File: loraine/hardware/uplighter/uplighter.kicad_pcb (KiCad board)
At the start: 2 copper layers, 49.5 x 49.5 mm, 10 parts, among them K1 CONN_3, K2 CONN_3, K3 CONN_3, U1 TL4242, U2 TL4242, U3 TL4242

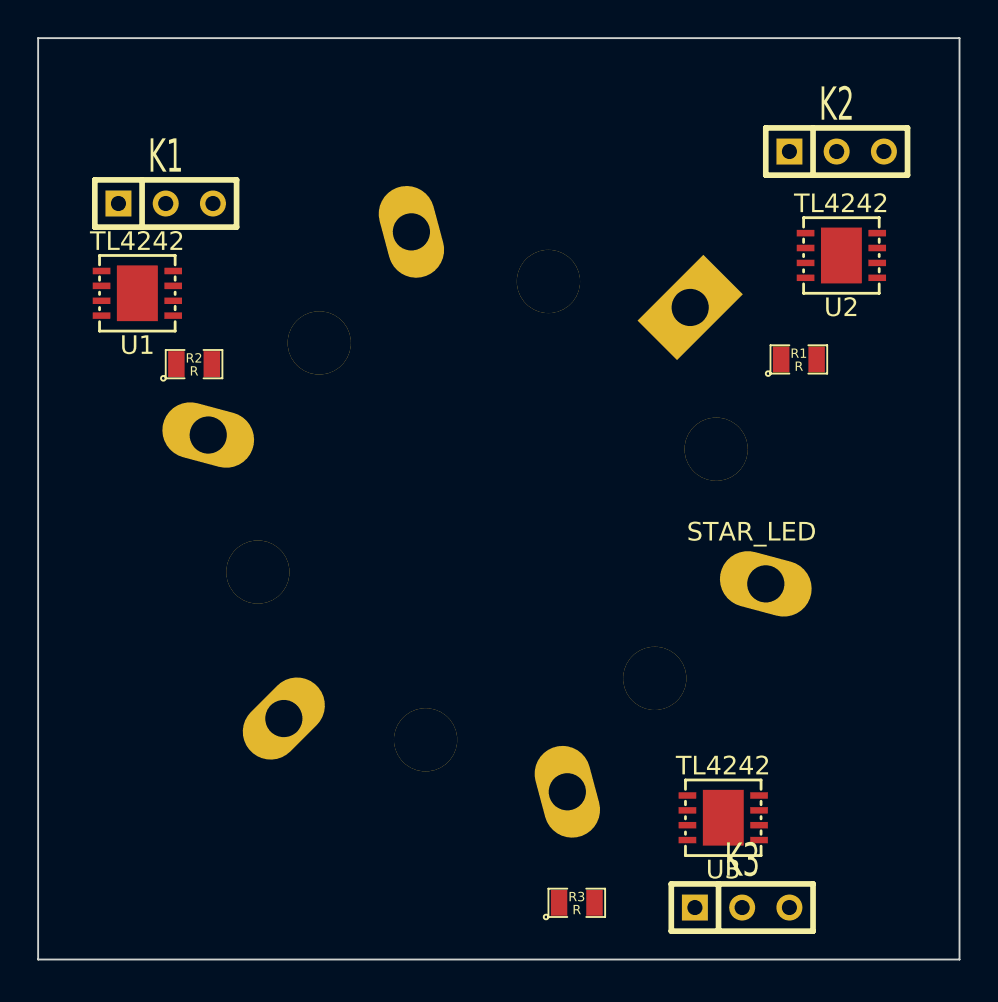
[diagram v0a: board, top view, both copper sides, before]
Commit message: Proposed output driver for node h/w
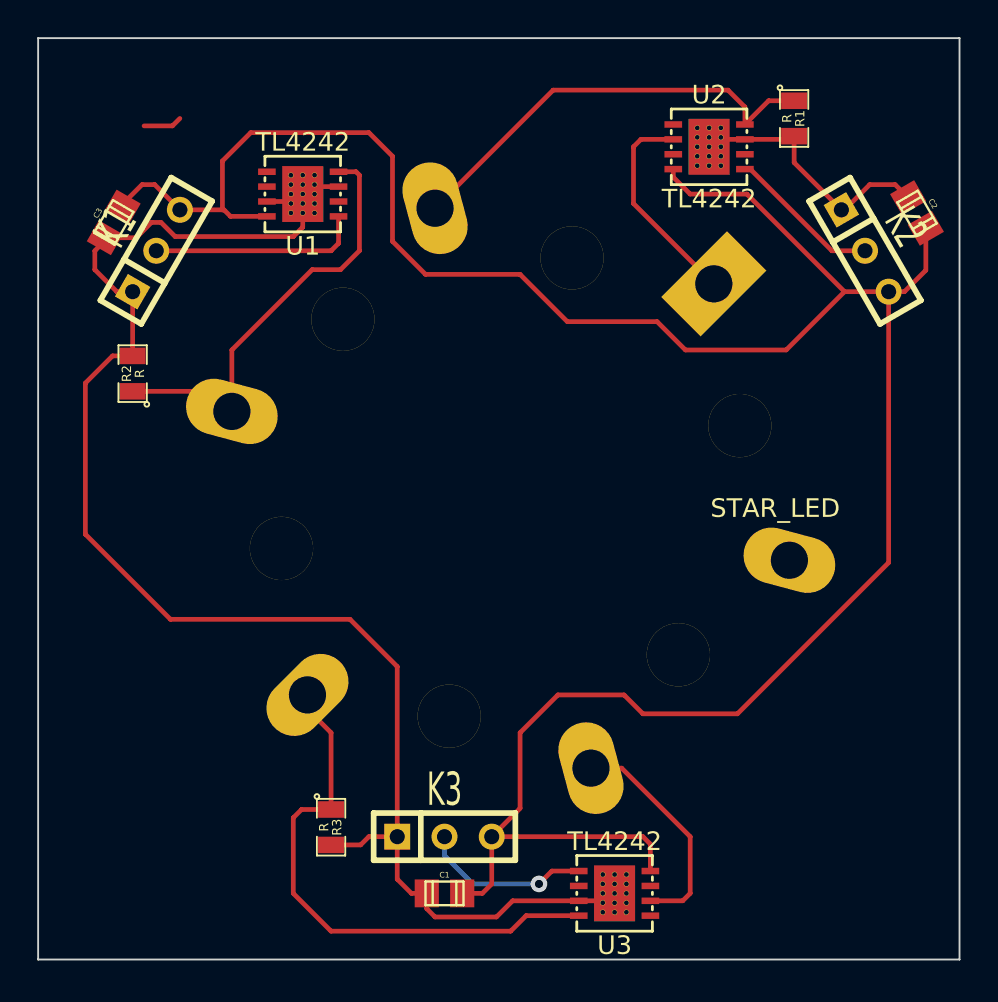
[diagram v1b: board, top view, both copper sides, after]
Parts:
- added C1: C, Capacitors_SMD:c_0805, F.Cu at (220.0, 87.9)
- added C2: C, Capacitors_SMD:c_0805, F.Cu at (245.4, 51.3)
- added C3: C, Capacitors_SMD:c_0805, F.Cu at (202.2, 51.8)
- moved K3 16.4 mm to (220.0, 84.8)
- moved R3 13.8 mm to (213.9, 84.3), turned to 270 degrees
- moved R1 13.0 mm to (238.8, 46.2), turned to 270 degrees
- moved U1 10.4 mm to (212.3, 50.3)
- moved U2 9.20 mm to (234.2, 47.8), turned to 180 degrees
- moved U3 7.12 mm to (229.1, 87.9)
- moved K2 5.55 mm to (242.6, 53.3), turned to 300 degrees
- moved R2 3.34 mm to (203.2, 59.9), turned to 90 degrees
- moved K1 2.59 mm to (204.5, 53.3), turned to 60 degrees
- moved D1 1.80 mm to (223.5, 66.0)
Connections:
- K1 pad 3: Net-(K1-Pad3) -> +5V
- K2 pad 3: Net-(K2-Pad3) -> +5V
- K3 pad 3: Net-(K3-Pad3) -> +5V
- U1 pad 8: Net-(K1-Pad3) -> +5V
- U2 pad 8: Net-(K2-Pad3) -> +5V
- U3 pad 8: Net-(K3-Pad3) -> +5V
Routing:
- net +5V: track 0.00 -> 127.5 mm
- net GND: track 0.00 -> 99.3 mm
- net /REF_RED: track 0.00 -> 29.8 mm
- net /REF_BLUE: track 0.00 -> 29.5 mm
- net /REF_GREEN: track 0.00 -> 23.8 mm
- net /LED_BLUE: track 0.00 -> 12.2 mm
- net /LED_GREEN: track 0.00 -> 11.5 mm
- net Net-(K1-Pad2): track 0.00 -> 10.2 mm
- net Net-(K3-Pad2): track 0.00 -> 9.15 mm, vias 0 -> 1
- net Net-(K2-Pad2): track 0.00 -> 8.27 mm
- net (no net): track 0.00 -> 2.09 mm
- net Net-(U1-Pad5): track 0.00 -> 1.45 mm

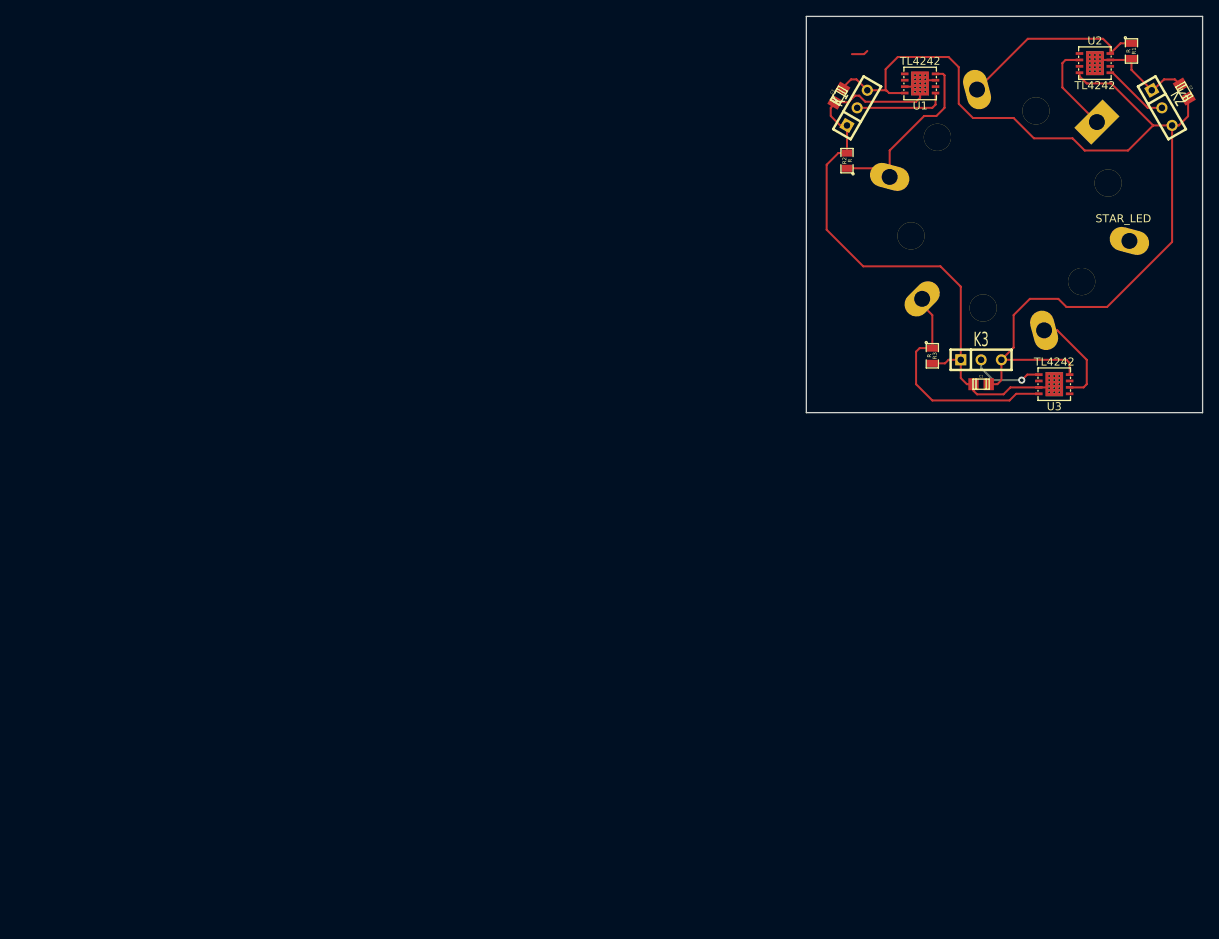
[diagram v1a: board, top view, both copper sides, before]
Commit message: Node PCB redo
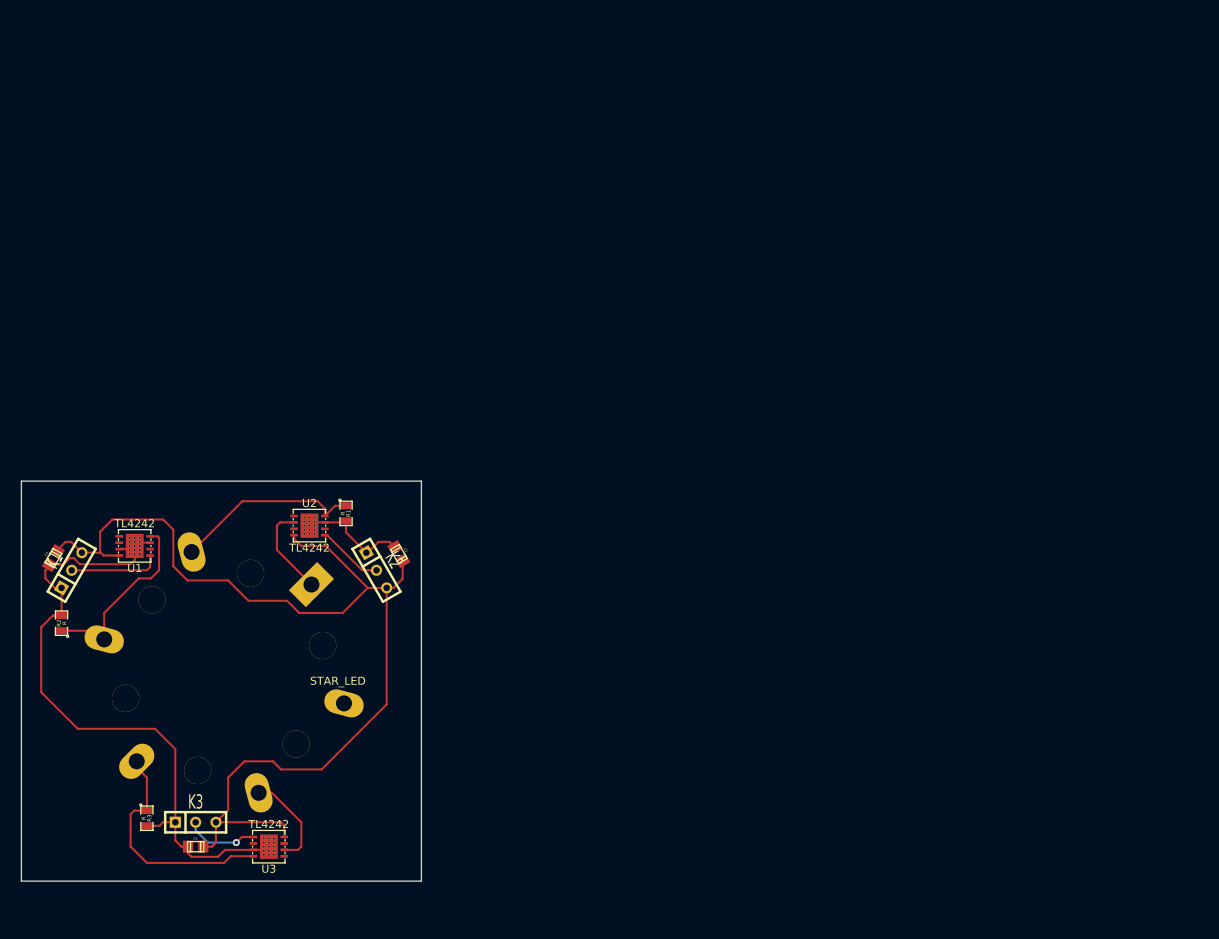
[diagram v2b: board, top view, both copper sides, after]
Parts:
- moved U3 113.9 mm to (130.9, 145.7)
- moved C1 113.9 mm to (121.8, 145.7)
- moved C2 113.9 mm to (147.2, 109.1)
- moved D1 113.9 mm to (125.3, 123.8)
- moved K2 113.9 mm to (144.4, 111.1)
- moved K3 113.9 mm to (121.8, 142.6)
- moved C3 113.9 mm to (104.0, 109.6)
- moved K1 113.9 mm to (106.3, 111.1)
- moved R1 113.9 mm to (140.6, 104.0)
- moved R2 113.9 mm to (105.0, 117.8)
- moved R3 113.9 mm to (115.7, 142.1)
- moved U1 113.9 mm to (114.2, 108.1)
- moved U2 113.9 mm to (136.0, 105.6)
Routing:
- net /REF_RED: track 29.8 -> 77.7 mm
- net +5V: track 127.5 -> 79.6 mm
- net (no net): track 2.09 -> 0.00 mm
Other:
- board size 49.5 x 49.5 mm -> 50 x 50 mm

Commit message: Finished both PCBs apart from logos and checking
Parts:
- C1, C2, C3: value C -> 100n
- moved C1 15.2 mm to (136.9, 143.9)
- moved C3 12.2 mm to (115.2, 104.8), turned to 0 degrees
- moved C2 11.0 mm to (136.4, 106.9), turned to 180 degrees
- moved K2 6.15 mm to (144.4, 105.0)
- moved U3 5.55 mm to (136.3, 147.2)
- moved U2 1.93 mm to (136.1, 103.6)
- moved R1 1.32 mm to (140.0, 102.9)
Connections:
- net +5V renamed VCC
- U1 pad 2: Net-(U1-Pad2) -> (no net)
- U1 pad 5: Net-(U1-Pad5) -> (no net)
- U1 pad 7: Net-(U1-Pad7) -> (no net)
- U2 pad 2: Net-(U2-Pad2) -> (no net)
- U2 pad 5: Net-(U2-Pad5) -> (no net)
- U2 pad 7: Net-(U2-Pad7) -> (no net)
- U3 pad 2: Net-(U3-Pad2) -> (no net)
- U3 pad 5: Net-(U3-Pad5) -> (no net)
- U3 pad 7: Net-(U3-Pad7) -> (no net)
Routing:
- net GND: track 99.3 -> 221.4 mm, vias 0 -> 9
- net VCC: track 79.6 -> 153.0 mm
- net /REF_RED: track 77.7 -> 17.0 mm
- net /LED_RED: track 0.00 -> 33.3 mm
- net /LED_BLUE: track 12.2 -> 18.8 mm
- net Net-(K3-Pad2): track 9.15 -> 14.2 mm, vias 1 -> 0
- net /REF_BLUE: track 29.5 -> 33.8 mm
- net /LED_GREEN: track 11.5 -> 13.8 mm
- net Net-(K1-Pad2): track 10.2 -> 7.96 mm
- net Net-(K2-Pad2): track 8.27 -> 6.39 mm
- net Net-(U1-Pad5): track 1.45 -> 0.00 mm
- net /REF_GREEN: track 23.8 -> 24.9 mm
- added copper zone on B.Cu, net GND
- added copper zone on F.Cu, net GND

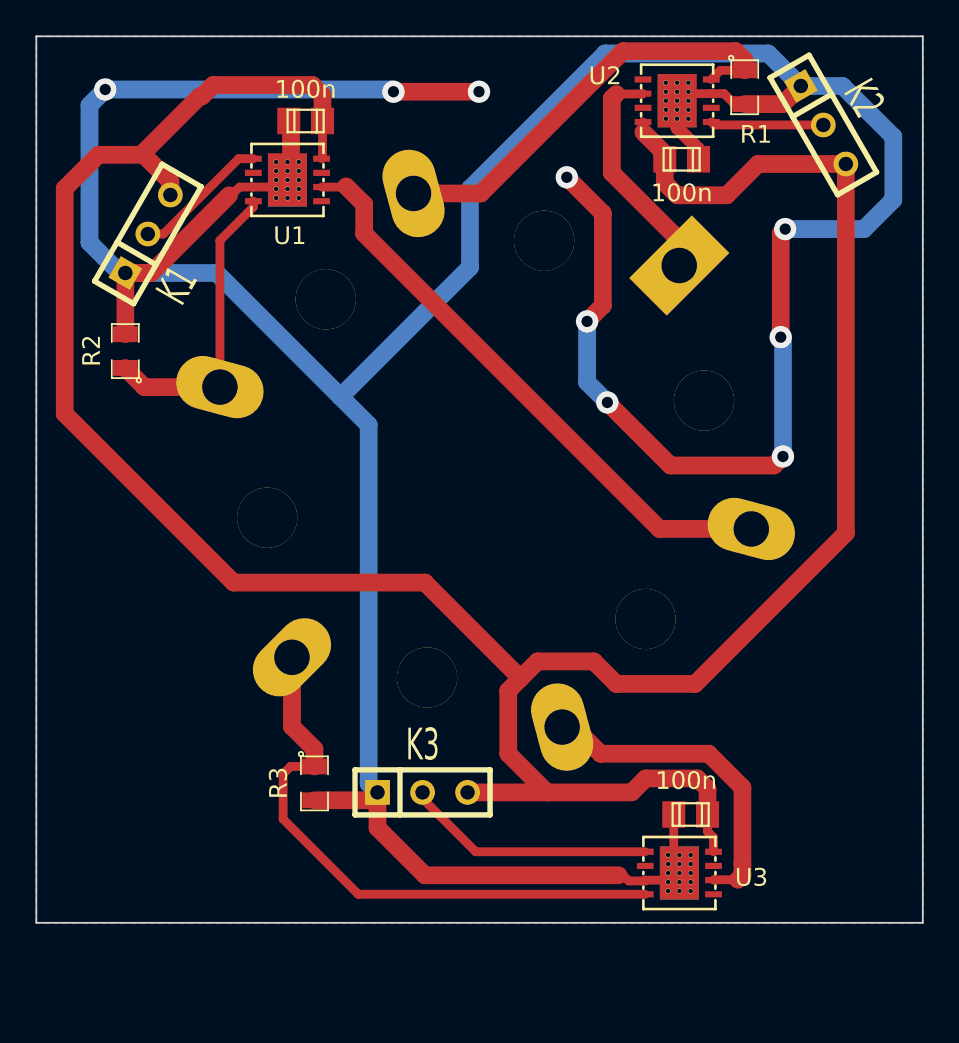
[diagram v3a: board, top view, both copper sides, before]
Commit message: 5V power conn on uplighter board
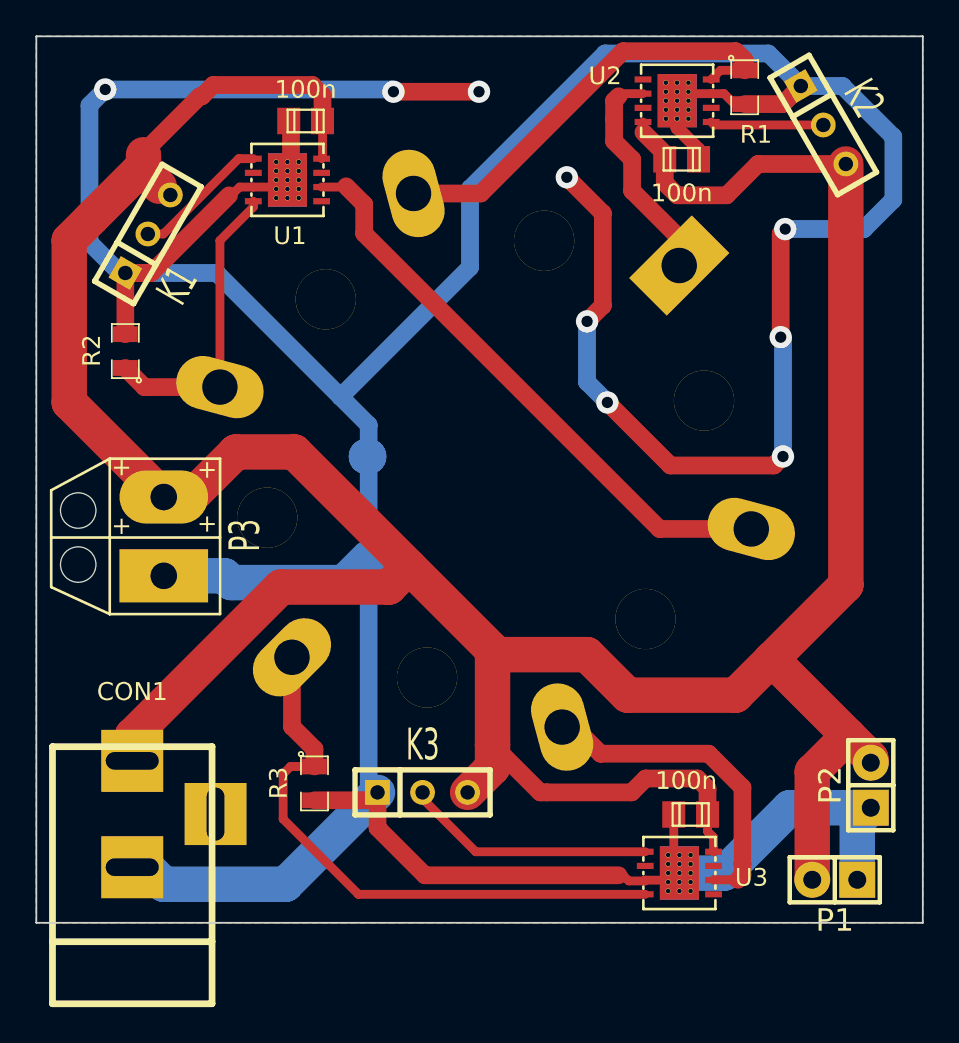
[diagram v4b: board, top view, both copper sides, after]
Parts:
- added CON1: BARREL_JACK, Connect:BARREL_JACK, F.Cu at (105.4, 147.1)
- added P1: POWER_THRU, Pin_Headers:Pin_Header_Straight_1x02, F.Cu at (145.0, 147.6)
- added P2: POWER, Pin_Headers:Pin_Header_Straight_1x02, F.Cu at (147.1, 142.2)
- added P3: SOLDER_PAD, solder_pad:SIL-2, F.Cu at (107.2, 128.3)
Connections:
- net VCC renamed +5V
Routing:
- net GND: track 221.4 -> 267.0 mm
- net +5V: track 153.0 -> 192.4 mm
- net /LED_GREEN: track 13.8 -> 15.3 mm

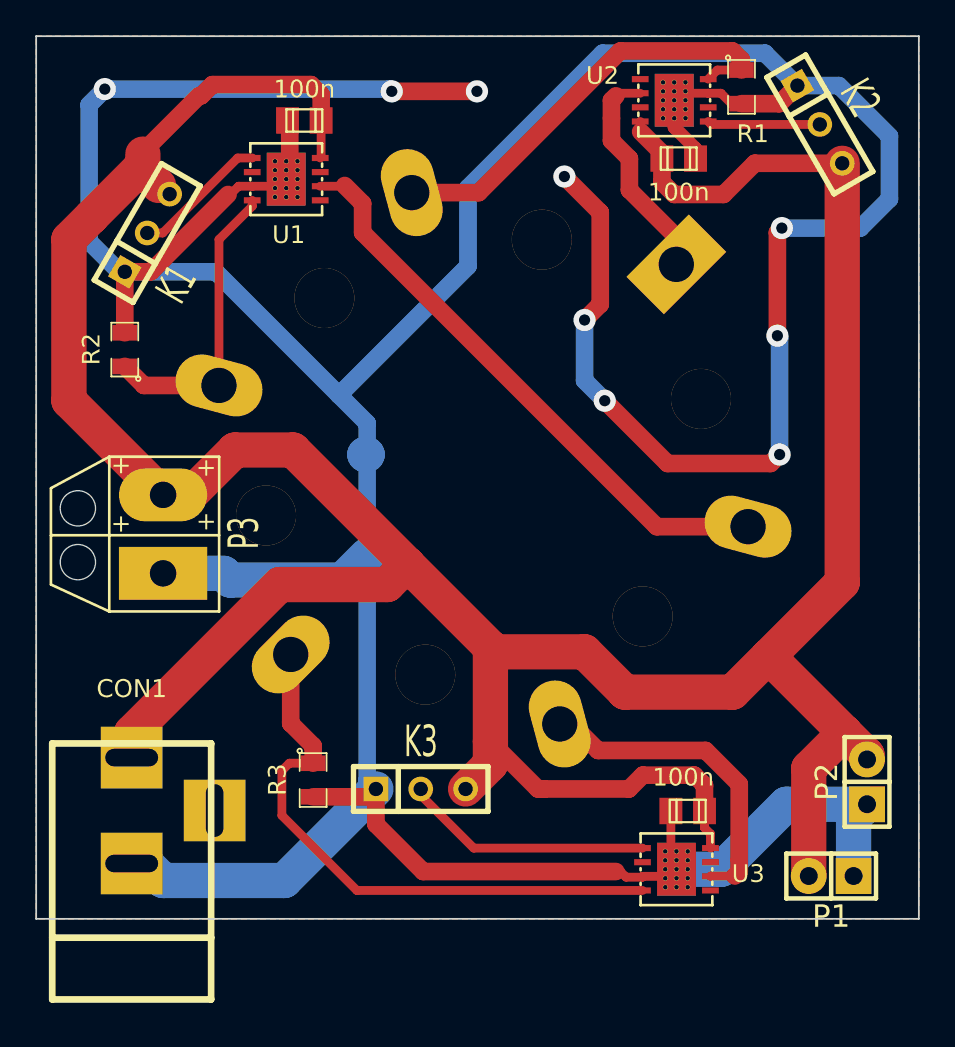
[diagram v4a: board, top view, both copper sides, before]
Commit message: Re-layed-out and rerouted uplighter pcb
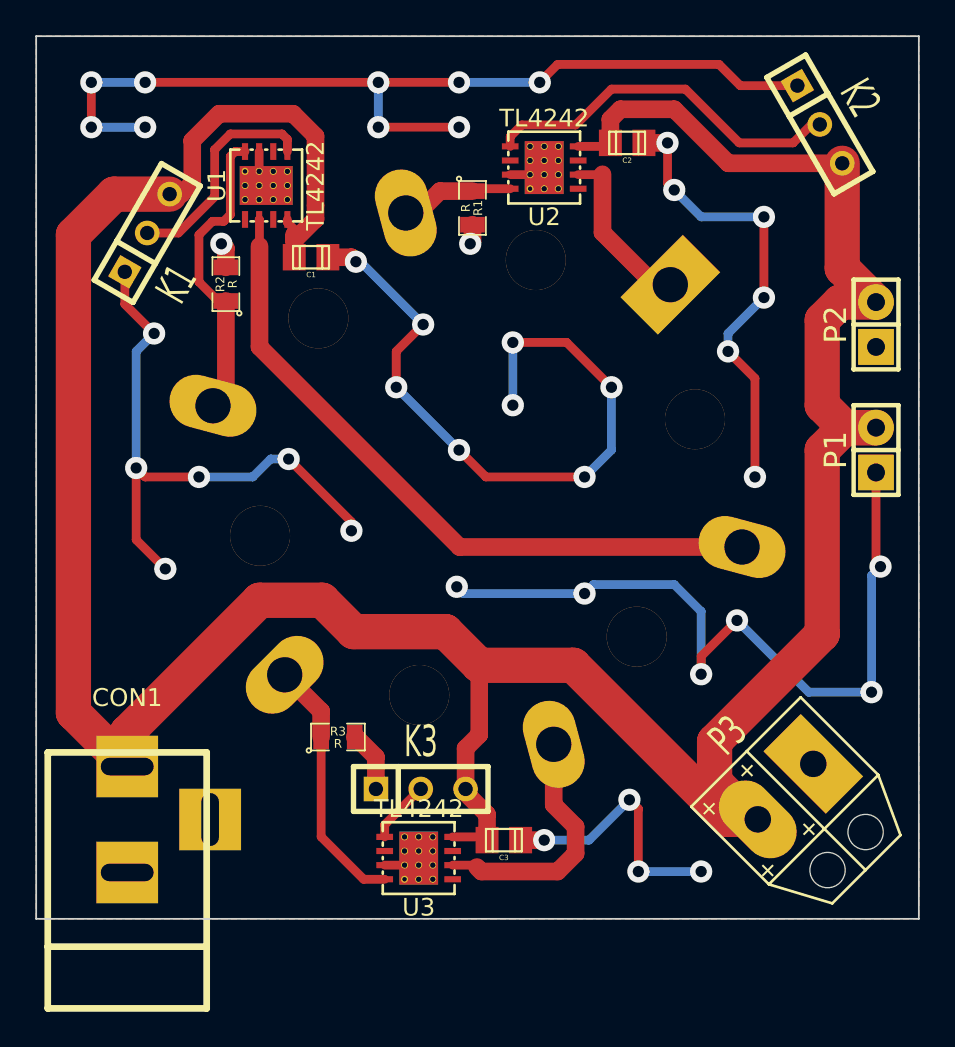
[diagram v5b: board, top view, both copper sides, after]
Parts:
- moved C3 42.3 mm to (126.5, 145.5), turned to 180 degrees
- moved P3 38.2 mm to (142.5, 142.7), turned to 225 degrees
- moved C1 37.9 mm to (115.6, 112.5), turned to 180 degrees
- moved P2 25.9 mm to (147.6, 116.3)
- moved P1 24.3 mm to (147.6, 123.4), turned to 90 degrees
- moved R1 16.7 mm to (124.7, 109.7)
- moved U3 14.6 mm to (121.7, 146.6)
- moved U2 8.29 mm to (128.8, 107.4), turned to 0 degrees
- moved R2 6.82 mm to (110.7, 114.0)
- moved C2 3.05 mm to (133.5, 106.0)
- moved R3 2.81 mm to (117.1, 139.7), turned to 0 degrees
- moved D1 1.20 mm to (125.0, 125.0)
- moved U1 1.19 mm to (113.0, 108.5), turned to 270 degrees
- moved CON1 0.57 mm to (105.2, 147.6)
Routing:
- net GND: track 267.0 -> 225.5 mm, vias 9 -> 41
- net /REF_BLUE: track 33.8 -> 14.6 mm
- net /REF_GREEN: track 24.9 -> 6.49 mm
- net Net-(K2-Pad2): track 6.39 -> 20.9 mm
- net Net-(K3-Pad2): track 14.2 -> 3.57 mm
- net /LED_RED: track 33.3 -> 39.3 mm
- net /LED_GREEN: track 15.3 -> 9.76 mm
- net +5V: track 192.4 -> 186.9 mm
- net Net-(K1-Pad2): track 7.96 -> 12.6 mm
- net /LED_BLUE: track 18.8 -> 14.2 mm
